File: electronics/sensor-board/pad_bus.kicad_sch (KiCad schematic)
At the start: 5 parts

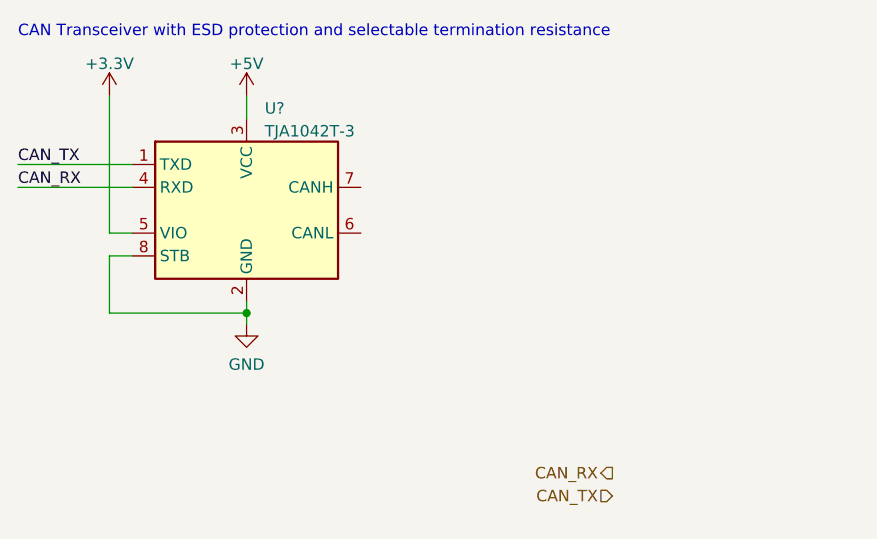
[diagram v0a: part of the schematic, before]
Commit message: LED output, debug and minor controller changes
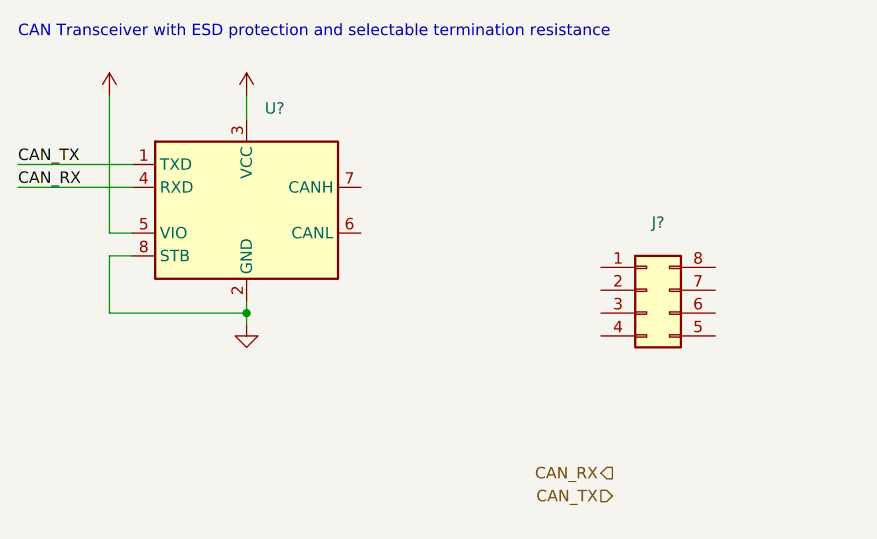
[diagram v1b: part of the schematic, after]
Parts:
- added J?: Conn_02x04_Counter_Clockwise, symbol Connector_Generic:Conn_02x04_Counter_Clockwise
- SW? (x4): value SW_DIP_x02 -> (none)
- U?: value TJA1042T-3 -> (none); footprint Package_SO:SOIC-8_3.9x4.9mm_P1.27mm -> (none)
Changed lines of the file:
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@@
     (effects (font (size 1.27 1.27)) (justify right))
+  )
+  (symbol (lib_id "Connector_Generic:Conn_02x04_Counter_Clockwise") (at 147.32 80.01 0) (unit 1)
+    (in_bom yes) (on_board yes) (fields_autoplaced)
+    (property "Reference" "J?" (id 0) (at 148.59 72.5002 0))
+    (property "Value" "Conn_02x04_Counter_Clockwise" (id 1) (at 148.59 75.0371 0)
+      (effects (font (size 1.27 1.27)) hide)
+    )
+    (property "Footprint" "" (id 2) (at 147.32 80.01 0)
+      (effects (font (size 1.27 1.27)) hide)
+    )
+    (property "Datasheet" "~" (id 3) (at 147.32 80.01 0)
+      (effects (font (size 1.27 1.27)) hide)
+    )
+    (pin "1")
+    (pin "2")
+    (pin "3")
+    (pin "4")
+    (pin "5")
+    (pin "6")
+    (pin "7")
+    (pin "8")
   )
   (symbol (lib_id "power:GND") (at 102.87 83.82 0) (unit 1)
@@
       (effects (font (size 1.27 1.27)) hide)
     )
-    (property "Value" "GND" (id 1) (at 102.87 88.2634 0))
+    (property "Value" "" (id 1) (at 102.87 88.2634 0))
     (property "Footprint" "" (id 2) (at 102.87 83.82 0)
       (effects (font (size 1.27 1.27)) hide)
@@
     (in_bom yes) (on_board yes)
     (property "Reference" "SW?" (id 0) (at 200.66 121.92 0))
-    (property "Value" "SW_DIP_x02" (id 1) (at 201.93 122.0271 0)
+    (property "Value" "" (id 1) (at 201.93 122.0271 0)
       (effects (font (size 1.27 1.27)) hide)
     )
@@
     (in_bom yes) (on_board yes)
     (property "Reference" "SW?" (id 0) (at 200.66 107.95 0))
-    (property "Value" "SW_DIP_x02" (id 1) (at 201.93 108.0571 0)
+    (property "Value" "" (id 1) (at 201.93 108.0571 0)
       (effects (font (size 1.27 1.27)) hide)
     )
@@
     (in_bom yes) (on_board yes)
     (property "Reference" "SW?" (id 0) (at 200.66 80.01 0))
-    (property "Value" "SW_DIP_x02" (id 1) (at 201.93 80.1171 0)
+    (property "Value" "" (id 1) (at 201.93 80.1171 0)
       (effects (font (size 1.27 1.27)) hide)
     )
@@
       (effects (font (size 1.27 1.27)) hide)
     )
-    (property "Value" "+5V" (id 1) (at 102.87 54.8442 0))
+    (property "Value" "" (id 1) (at 102.87 54.8442 0))
     (property "Footprint" "" (id 2) (at 102.87 58.42 0)
       (effects (font (size 1.27 1.27)) hide)
@@
       (effects (font (size 1.27 1.27)) (justify left))
     )
-    (property "Value" "TJA1042T-3" (id 1) (at 104.8894 62.3371 0)
+    (property "Value" "" (id 1) (at 104.8894 62.3371 0)
       (effects (font (size 1.27 1.27)) (justify left))
     )
-    (property "Footprint" "Package_SO:SOIC-8_3.9x4.9mm_P1.27mm" (id 2) (at 102.87 83.82 0)
+    (property "Footprint" "" (id 2) (at 102.87 83.82 0)
       (effects (font (size 1.27 1.27) italic) hide)
     )
@@
       (effects (font (size 1.27 1.27)) hide)
     )
-    (property "Value" "+3.3V" (id 1) (at 87.63 54.8442 0))
+    (property "Value" "" (id 1) (at 87.63 54.8442 0))
     (property "Footprint" "" (id 2) (at 87.63 58.42 0)
       (effects (font (size 1.27 1.27)) hide)
@@
     (in_bom yes) (on_board yes)
     (property "Reference" "SW?" (id 0) (at 200.66 93.98 0))
-    (property "Value" "SW_DIP_x02" (id 1) (at 201.93 94.0871 0)
+    (property "Value" "" (id 1) (at 201.93 94.0871 0)
       (effects (font (size 1.27 1.27)) hide)
     )

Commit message: Build Pad Bus and annotate
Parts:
- removed SW? (x2): (no value), symbol Switch:SW_DIP_x02
- added C38, C39: 100n, symbol Device:C_Small
- added C40, C42, C43, C45: 100p, symbol Device:C_Small
- added C41, C44: 4.7n, symbol Device:C_Small
- added J14, J15, J16: (no value), symbol Connector_Generic:Conn_02x04_Counter_Clockwise
- added R46, R47, R50, R51: 27R, symbol Device:R_Small
- added R48, R49, R52, R53: 33R, symbol Device:R_Small
- added SW10, SW8, SW9: (no value), symbol Switch:SW_DIP_x02
- added SW11: SW_DIP_x02, symbol Switch:SW_DIP_x02
- SW12, SW7: renamed from SW?; value (none) -> SW_DIP_x02
- U10: renamed from U?; value (none) -> TJA1042T-3; footprint (none) -> Package_SO:SOIC-8_3.9x4.9mm_P1.27mm
- gave numbers to parts that had none: 1
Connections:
- net +3.3V: now also C38.1
- net +5V: now also C38.2, C39.2
- net GND: now also J13.3 (Pin_3), J13.4 (Pin_4), C39.1, C40.2, C41.2, C42.2, C43.2, C44.2, C45.2, J14.3 (Pin_3), J14.4 (Pin_4), J15.3 (Pin_3), J15.4 (Pin_4), J16.3 (Pin_3), J16.4 (Pin_4)
- net +24V: now reaches J13.1 (Pin_1)
- net +24V: now also J13.2 (Pin_2), J14.1 (Pin_1), J14.2 (Pin_2), J15.1 (Pin_1), J15.2 (Pin_2), J16.1 (Pin_1), J16.2 (Pin_2)
- net CANL: now reaches J13.5 (Pin_5)
- net CANL: now also SW12.2, SW7.3, U10.6 (CANL), J14.7 (Pin_7), SW8.2
- net CANH: now reaches J13.6 (Pin_6)
- net CANH: now also SW12.1, SW7.4, U10.7 (CANH), J14.8 (Pin_8), SW8.1
- net at J13.7 (Pin_7): now also SW7.2, J16.5 (Pin_5), SW10.3, SW11.2
- net at J13.8 (Pin_8): now also SW7.1, J16.6 (Pin_6), SW10.4, SW11.1
- net at SW12.3: now also R51.1
- net at SW12.4: now also R50.1
- new net: R46.1, SW11.4
- new net: R46.2, R48.1
- new net: C43.1, C44.1, C45.1, R52.2, R53.2
- new net: J14.5 (Pin_5), J15.7 (Pin_7), SW8.3, SW9.2
- new net: J14.6 (Pin_6), J15.8 (Pin_8), SW8.4, SW9.1
- new net: J15.5 (Pin_5), J16.7 (Pin_7), SW10.2, SW9.3
- new net: J15.6 (Pin_6), J16.8 (Pin_8), SW10.1, SW9.4
- new net: R47.2, R49.1
- new net: C40.1, C41.1, C42.1, R48.2, R49.2
- new net: R50.2, R52.1
- new net: R51.2, R53.1
- new net: R47.1, SW11.3
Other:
- note added: "CAN Transceiver with selectable termination"
- note added: "Circular Pad Bus with selectable end termination"
- note added: "Down Bus Connector"
- note added: "Left Bus Connector"
- note added: "Right Bus Connector"
- note added: "Up Bus Connector"
- note removed: "CAN Transceiver with ESD protection and selectable termination resistance"
- moved on the sheet: J13, SW12, SW7, U10

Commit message: Minor tweaks, footprints added
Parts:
- C38, C39, C40, C41, C42, C43, C44, C45: footprint (none) -> Capacitor_SMD:C_0603_1608Metric
- J13: footprint (none) -> Connector_PinHeader_2.54mm:PinHeader_2x04_P2.54mm_Vertical
- J14, J15, J16: value (none) -> Conn_02x04_Counter_Clockwise; footprint (none) -> Connector_PinHeader_2.54mm:PinHeader_2x04_P2.54mm_Vertical
- R46, R47, R48, R49, R50, R51, R52, R53: footprint (none) -> Resistor_SMD:R_0603_1608Metric
- SW10, SW8, SW9: value (none) -> SW_DIP_x02; footprint (none) -> Button_Switch_THT:SW_DIP_SPSTx02_Slide_6.7x6.64mm_W7.62mm_P2.54mm_LowProfile
- SW11, SW12, SW7: footprint (none) -> Button_Switch_THT:SW_DIP_SPSTx02_Slide_6.7x6.64mm_W7.62mm_P2.54mm_LowProfile
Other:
- note added: "CAN Transceiver with selectable start termination"
- note removed: "CAN Transceiver with selectable termination"

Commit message: Final tweaks and schematic review complete
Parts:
- removed J13, J14, J15, J16: Conn_02x04_Counter_Clockwise, Connector_PinHeader_2.54mm:PinHeader_2x04_P2.54mm_Vertical, symbol Connector_Generic:Conn_02x04_Counter_Clockwise
- added H1, H2, H3, H4: MountingHole_Pad, MountingHole:MountingHole_3.2mm_M3_Pad, symbol Mechanical:MountingHole_Pad
- added J13, J14, J15, J16: Conn_02x04_Odd_Even, Connector_PinHeader_2.54mm:PinHeader_2x04_P2.54mm_Vertical, symbol Connector_Generic:Conn_02x04_Odd_Even
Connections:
- net +24V: now also J13.1 (Pin_1), J13.3 (Pin_3), J14.1 (Pin_1), J14.3 (Pin_3), J15.1 (Pin_1), J15.3 (Pin_3), J16.1 (Pin_1), J16.3 (Pin_3)
- net CANH: now also J13.6 (Pin_6), J14.2 (Pin_2)
- net CANL: now also J13.8 (Pin_8), J14.4 (Pin_4)
- net GND: now also J13.5 (Pin_5), J13.7 (Pin_7), J14.5 (Pin_5), J14.7 (Pin_7), J15.5 (Pin_5), J15.7 (Pin_7), J16.5 (Pin_5), J16.7 (Pin_7)
- net at SW8.3, SW9.2: now also J14.8 (Pin_8), J15.4 (Pin_4)
- net at SW8.4, SW9.1: now also J14.6 (Pin_6), J15.2 (Pin_2)
- net at SW10.3, SW11.2, SW7.2: now also J13.4 (Pin_4), J16.8 (Pin_8)
- net at SW10.4, SW11.1, SW7.1: now also J13.2 (Pin_2), J16.6 (Pin_6)
- net at SW10.2, SW9.3: now also J15.8 (Pin_8), J16.4 (Pin_4)
- net at SW10.1, SW9.4: now also J15.6 (Pin_6), J16.2 (Pin_2)
- no-connect marks 0 -> 4

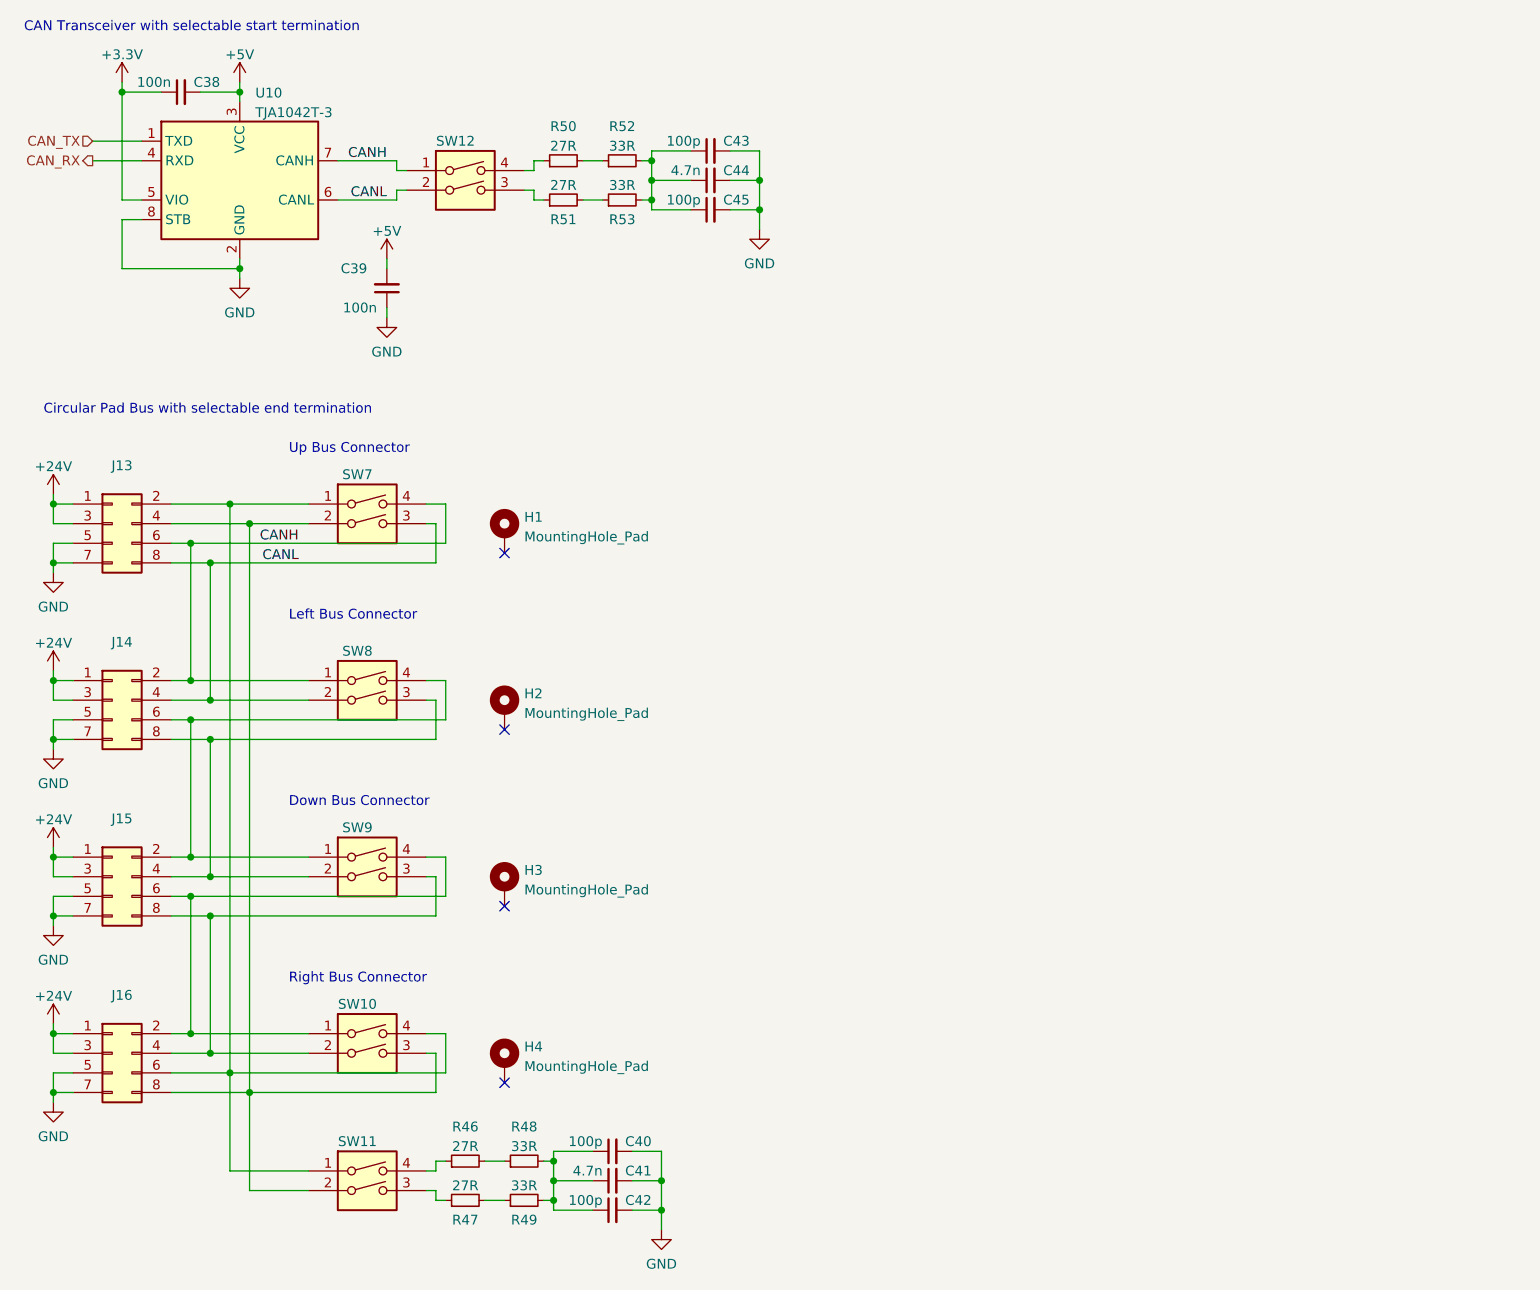
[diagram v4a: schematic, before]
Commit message: Remove DIP switches and re-organize CAN connectors
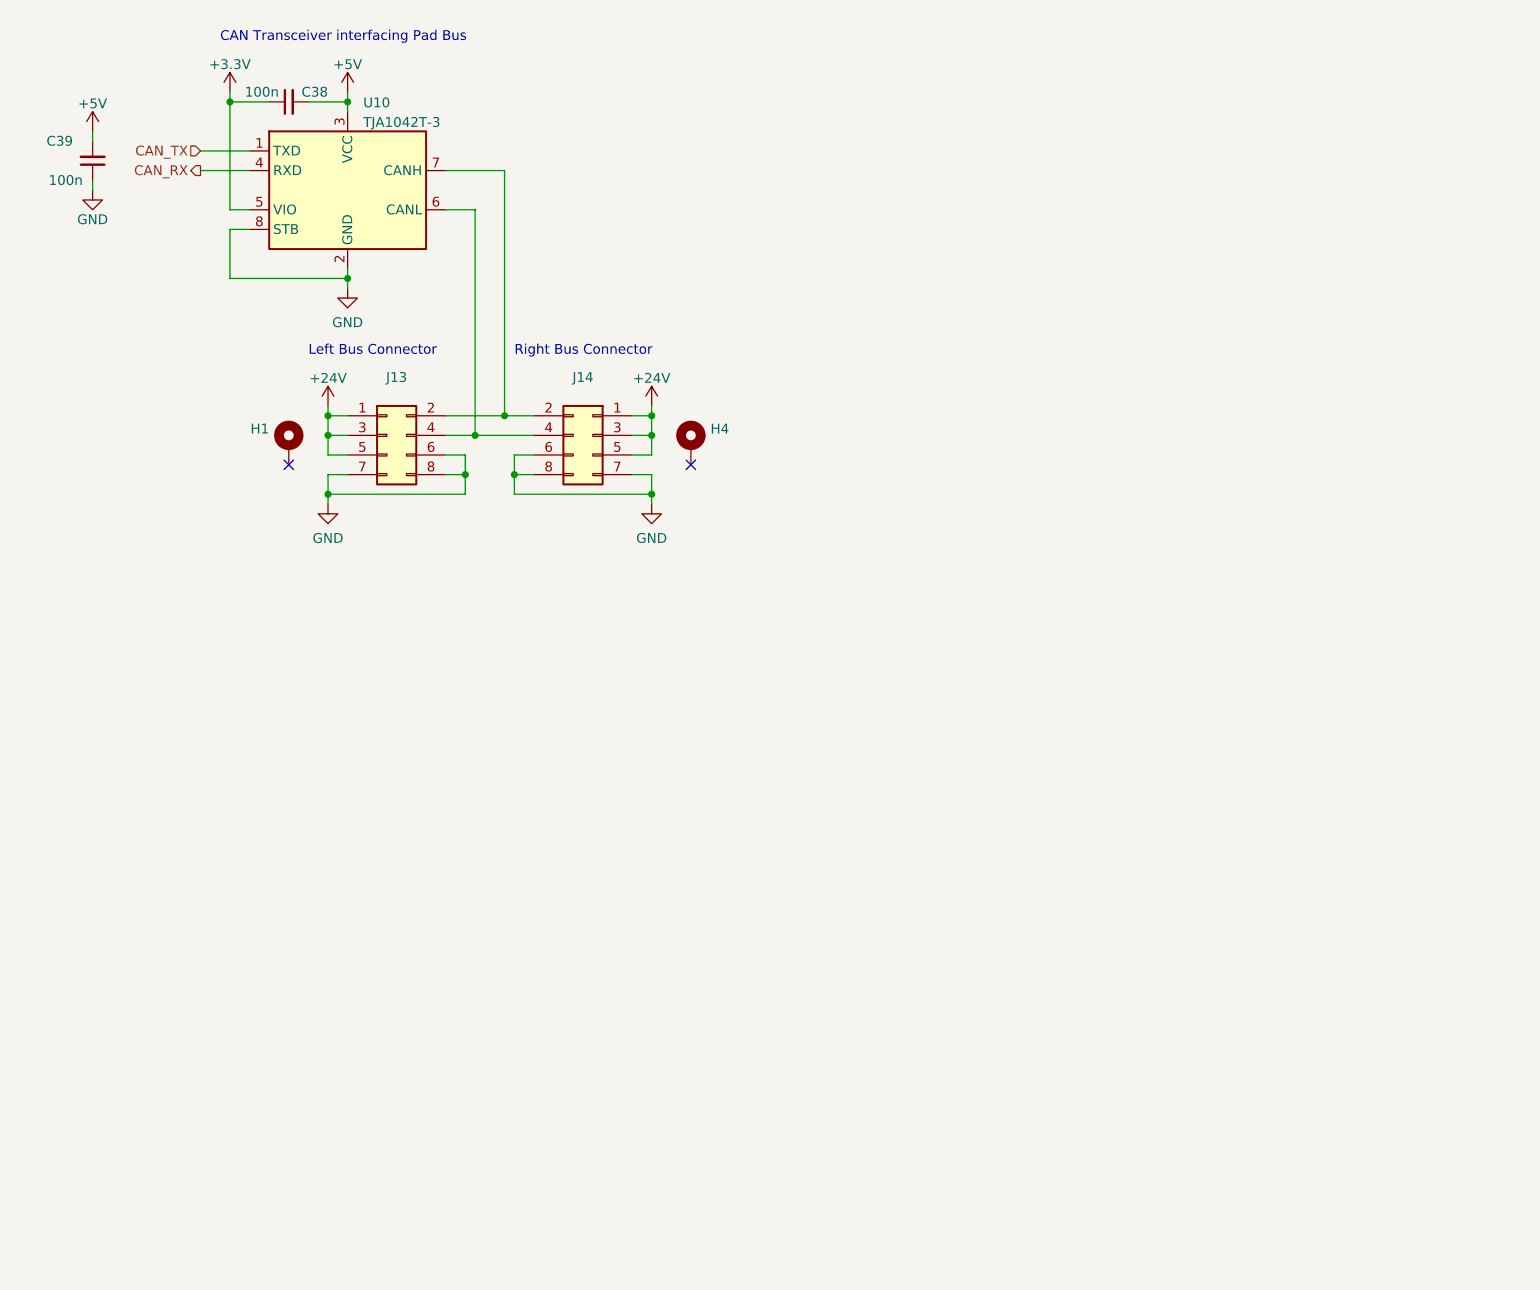
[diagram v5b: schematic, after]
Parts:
- removed C40, C42, C43, C45: 100p, Capacitor_SMD:C_0603_1608Metric, symbol Device:C_Small
- removed C41, C44: 4.7n, Capacitor_SMD:C_0603_1608Metric, symbol Device:C_Small
- removed H2, H3: MountingHole_Pad, MountingHole:MountingHole_3.2mm_M3_Pad, symbol Mechanical:MountingHole_Pad
- removed J15, J16: Conn_02x04_Odd_Even, Connector_PinHeader_2.54mm:PinHeader_2x04_P2.54mm_Vertical, symbol Connector_Generic:Conn_02x04_Odd_Even
- removed R46, R47, R50, R51: 27R, Resistor_SMD:R_0603_1608Metric, symbol Device:R_Small
- removed R48, R49, R52, R53: 33R, Resistor_SMD:R_0603_1608Metric, symbol Device:R_Small
- removed SW10, SW11, SW12, SW7, SW8, SW9: SW_DIP_x02, Button_Switch_THT:SW_DIP_SPSTx02_Slide_6.7x6.64mm_W7.62mm_P2.54mm_LowProfile, symbol Switch:SW_DIP_x02
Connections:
- net +24V: now also J13.5 (Pin_5), J14.5 (Pin_5)
- net GND: now also J13.6 (Pin_6), J13.8 (Pin_8), J14.6 (Pin_6), J14.8 (Pin_8); no longer J13.5 (Pin_5), J14.5 (Pin_5)
- net at J13.4 (Pin_4): now also J14.4 (Pin_4), U10.6 (CANL)
- net at J13.2 (Pin_2): now also J14.2 (Pin_2), U10.7 (CANH)
- removed net CANH: J13.6 (Pin_6), J14.2 (Pin_2), U10.7 (CANH)
- removed net CANL: J13.8 (Pin_8), J14.4 (Pin_4), U10.6 (CANL)
- no-connect marks 4 -> 2
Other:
- note added: "CAN Transceiver interfacing Pad Bus"
- note removed: "CAN Transceiver with selectable start termination"
- note removed: "Circular Pad Bus with selectable end termination"
- note removed: "Down Bus Connector"
- note removed: "Up Bus Connector"
- moved on the sheet: C38, C39, H4, U10
